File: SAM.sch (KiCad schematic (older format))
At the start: 60 parts, among them J301 CONN_02x05, 0.05\", SW301 Switch_DPST, SW302 Switch_DPST, U301 ATSAMD21J18A-MUT, U302 AAT4610, U303 AAT4610, X301 FC-135

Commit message: components and footprints
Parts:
- SW301, SW302: footprint (none) -> tm-kicad-lib:SPST-TH
- TP301, TP303, TP304, TP305, TP306, TP307, TP308, TP309, TP310, TP311, TP312, TP313, TP314, TP315, TP316, TP317, TP318, TP319, TP320, TP321, TP322, TP323, TP324: value 0914-0-15-20-77-14-11-0 -> 0932-0-15-20-77-14-11-0
- TP302: value 0914-0-15-20-77-14-11-0-0-15-20-77-14-11-0 -> 0932-0-15-20-77-14-11-0
- U302, U303: footprint (none) -> Housings_SOT-23_SOT-143_TSOT-6:SOT-23-5
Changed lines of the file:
@@
 P 8800 2300
 F 0 "TP322" H 8800 2350 60  0000 C CNN
-F 1 "0914-0-15-20-77-14-11-0" H 8800 2250 60  0001 C CNN
+F 1 "0932-0-15-20-77-14-11-0" H 8800 2250 60  0001 C CNN
 F 2 "tm-kicad-lib:Testpoint" H 8800 2300 60  0001 C CNN
 F 3 "" H 8800 2300 60  0000 C CNN
@@
 P 8800 2500
 F 0 "TP323" H 8800 2550 60  0000 C CNN
-F 1 "0914-0-15-20-77-14-11-0" H 8800 2450 60  0001 C CNN
+F 1 "0932-0-15-20-77-14-11-0" H 8800 2450 60  0001 C CNN
 F 2 "tm-kicad-lib:Testpoint" H 8800 2500 60  0001 C CNN
 F 3 "" H 8800 2500 60  0000 C CNN
@@
 P 8800 2100
 F 0 "TP321" H 8800 2150 60  0000 C CNN
-F 1 "0914-0-15-20-77-14-11-0" H 8800 2050 60  0001 C CNN
+F 1 "0932-0-15-20-77-14-11-0" H 8800 2050 60  0001 C CNN
 F 2 "tm-kicad-lib:Testpoint" H 8800 2100 60  0001 C CNN
 F 3 "" H 8800 2100 60  0000 C CNN
@@
 P 8800 1900
 F 0 "TP320" H 8800 1950 60  0000 C CNN
-F 1 "0914-0-15-20-77-14-11-0" H 8800 1850 60  0001 C CNN
+F 1 "0932-0-15-20-77-14-11-0" H 8800 1850 60  0001 C CNN
 F 2 "tm-kicad-lib:Testpoint" H 8800 1900 60  0001 C CNN
 F 3 "" H 8800 1900 60  0000 C CNN
@@
 P 8000 5500
 F 0 "TP302" H 8000 5550 60  0000 C CNN
-F 1 "0914-0-15-20-77-14-11-0-0-15-20-77-14-11-0" H 8000 5450 60  0001 C CNN
+F 1 "0932-0-15-20-77-14-11-0" H 8000 5450 60  0001 C CNN
 F 2 "tm-kicad-lib:Testpoint" H 8000 5500 60  0001 C CNN
 F 3 "" H 8000 5500 60  0000 C CNN
@@
 P 8000 5600
 F 0 "TP303" H 8000 5650 60  0000 C CNN
-F 1 "0914-0-15-20-77-14-11-0" H 8000 5550 60  0001 C CNN
+F 1 "0932-0-15-20-77-14-11-0" H 8000 5550 60  0001 C CNN
 F 2 "tm-kicad-lib:Testpoint" H 8000 5600 60  0001 C CNN
 F 3 "" H 8000 5600 60  0000 C CNN
@@
 P 8000 5800
 F 0 "TP305" H 8000 5850 60  0000 C CNN
-F 1 "0914-0-15-20-77-14-11-0" H 8000 5750 60  0001 C CNN
+F 1 "0932-0-15-20-77-14-11-0" H 8000 5750 60  0001 C CNN
 F 2 "tm-kicad-lib:Testpoint" H 8000 5800 60  0001 C CNN
 F 3 "" H 8000 5800 60  0000 C CNN
@@
 P 8000 6000
 F 0 "TP306" H 8000 6050 60  0000 C CNN
-F 1 "0914-0-15-20-77-14-11-0" H 8000 5950 60  0001 C CNN
+F 1 "0932-0-15-20-77-14-11-0" H 8000 5950 60  0001 C CNN
 F 2 "tm-kicad-lib:Testpoint" H 8000 6000 60  0001 C CNN
 F 3 "" H 8000 6000 60  0000 C CNN
@@
 P 8000 6100
 F 0 "TP307" H 8000 6150 60  0000 C CNN
-F 1 "0914-0-15-20-77-14-11-0" H 8000 6050 60  0001 C CNN
+F 1 "0932-0-15-20-77-14-11-0" H 8000 6050 60  0001 C CNN
 F 2 "tm-kicad-lib:Testpoint" H 8000 6100 60  0001 C CNN
 F 3 "" H 8000 6100 60  0000 C CNN
@@
 P 8000 6200
 F 0 "TP308" H 8000 6250 60  0000 C CNN
-F 1 "0914-0-15-20-77-14-11-0" H 8000 6150 60  0001 C CNN
+F 1 "0932-0-15-20-77-14-11-0" H 8000 6150 60  0001 C CNN
 F 2 "tm-kicad-lib:Testpoint" H 8000 6200 60  0001 C CNN
 F 3 "" H 8000 6200 60  0000 C CNN
@@
 P 8000 6300
 F 0 "TP309" H 8000 6350 60  0000 C CNN
-F 1 "0914-0-15-20-77-14-11-0" H 8000 6250 60  0001 C CNN
+F 1 "0932-0-15-20-77-14-11-0" H 8000 6250 60  0001 C CNN
 F 2 "tm-kicad-lib:Testpoint" H 8000 6300 60  0001 C CNN
 F 3 "" H 8000 6300 60  0000 C CNN
@@
 P 8000 6500
 F 0 "TP310" H 8000 6550 60  0000 C CNN
-F 1 "0914-0-15-20-77-14-11-0" H 8000 6450 60  0001 C CNN
+F 1 "0932-0-15-20-77-14-11-0" H 8000 6450 60  0001 C CNN
 F 2 "tm-kicad-lib:Testpoint" H 8000 6500 60  0001 C CNN
 F 3 "" H 8000 6500 60  0000 C CNN
@@
 P 8000 6600
 F 0 "TP311" H 8000 6650 60  0000 C CNN
-F 1 "0914-0-15-20-77-14-11-0" H 8000 6550 60  0001 C CNN
+F 1 "0932-0-15-20-77-14-11-0" H 8000 6550 60  0001 C CNN
 F 2 "tm-kicad-lib:Testpoint" H 8000 6600 60  0001 C CNN
 F 3 "" H 8000 6600 60  0000 C CNN
@@
 P 8000 6700
 F 0 "TP312" H 8000 6750 60  0000 C CNN
-F 1 "0914-0-15-20-77-14-11-0" H 8000 6650 60  0001 C CNN
+F 1 "0932-0-15-20-77-14-11-0" H 8000 6650 60  0001 C CNN
 F 2 "tm-kicad-lib:Testpoint" H 8000 6700 60  0001 C CNN
 F 3 "" H 8000 6700 60  0000 C CNN
@@
 P 8000 6800
 F 0 "TP313" H 8000 6850 60  0000 C CNN
-F 1 "0914-0-15-20-77-14-11-0" H 8000 6750 60  0001 C CNN
+F 1 "0932-0-15-20-77-14-11-0" H 8000 6750 60  0001 C CNN
 F 2 "tm-kicad-lib:Testpoint" H 8000 6800 60  0001 C CNN
 F 3 "" H 8000 6800 60  0000 C CNN
@@
 P 8000 8000
 F 0 "TP317" H 8000 8050 60  0000 C CNN
-F 1 "0914-0-15-20-77-14-11-0" H 8000 7950 60  0001 C CNN
+F 1 "0932-0-15-20-77-14-11-0" H 8000 7950 60  0001 C CNN
 F 2 "tm-kicad-lib:Testpoint" H 8000 8000 60  0001 C CNN
 F 3 "" H 8000 8000 60  0000 C CNN
@@
 P 8000 8100
 F 0 "TP318" H 8000 8150 60  0000 C CNN
-F 1 "0914-0-15-20-77-14-11-0" H 8000 8050 60  0001 C CNN
+F 1 "0932-0-15-20-77-14-11-0" H 8000 8050 60  0001 C CNN
 F 2 "tm-kicad-lib:Testpoint" H 8000 8100 60  0001 C CNN
 F 3 "" H 8000 8100 60  0000 C CNN
@@
 P 8000 7700
 F 0 "TP315" H 8000 7750 60  0000 C CNN
-F 1 "0914-0-15-20-77-14-11-0" H 8000 7650 60  0001 C CNN
+F 1 "0932-0-15-20-77-14-11-0" H 8000 7650 60  0001 C CNN
 F 2 "tm-kicad-lib:Testpoint" H 8000 7700 60  0001 C CNN
 F 3 "" H 8000 7700 60  0000 C CNN
@@
 P 8000 7800
 F 0 "TP316" H 8000 7850 60  0000 C CNN
-F 1 "0914-0-15-20-77-14-11-0" H 8000 7750 60  0001 C CNN
+F 1 "0932-0-15-20-77-14-11-0" H 8000 7750 60  0001 C CNN
 F 2 "tm-kicad-lib:Testpoint" H 8000 7800 60  0001 C CNN
 F 3 "" H 8000 7800 60  0000 C CNN
@@
 P 8000 7500
 F 0 "TP314" H 8000 7550 60  0000 C CNN
-F 1 "0914-0-15-20-77-14-11-0" H 8000 7450 60  0001 C CNN
+F 1 "0932-0-15-20-77-14-11-0" H 8000 7450 60  0001 C CNN
 F 2 "tm-kicad-lib:Testpoint" H 8000 7500 60  0001 C CNN
 F 3 "" H 8000 7500 60  0000 C CNN
@@
 P 2700 5900
 F 0 "TP301" H 2700 5950 60  0000 C CNN
-F 1 "0914-0-15-20-77-14-11-0" H 2700 5850 60  0001 C CNN
+F 1 "0932-0-15-20-77-14-11-0" H 2700 5850 60  0001 C CNN
 F 2 "tm-kicad-lib:Testpoint" H 2700 5900 60  0001 C CNN
 F 3 "" H 2700 5900 60  0000 C CNN
@@
 P 8000 5700
 F 0 "TP304" H 8000 5750 60  0000 C CNN
-F 1 "0914-0-15-20-77-14-11-0" H 8000 5650 60  0001 C CNN
+F 1 "0932-0-15-20-77-14-11-0" H 8000 5650 60  0001 C CNN
 F 2 "tm-kicad-lib:Testpoint" H 8000 5700 60  0001 C CNN
 F 3 "" H 8000 5700 60  0000 C CNN
@@
 F 0 "U302" H 14450 5750 60  0000 C CNN
 F 1 "AAT4610" H 14800 5500 60  0000 C CNN
-F 2 "" H 14800 5500 60  0000 C CNN
+F 2 "Housings_SOT-23_SOT-143_TSOT-6:SOT-23-5" H 14800 5500 60  0001 C CNN
 F 3 "" H 14800 5500 60  0000 C CNN
 	1    14800 5500
@@
 F 0 "U303" H 14450 7450 60  0000 C CNN
 F 1 "AAT4610" H 14800 7200 60  0000 C CNN
-F 2 "" H 14800 7200 60  0000 C CNN
+F 2 "Housings_SOT-23_SOT-143_TSOT-6:SOT-23-5" H 14800 7200 60  0001 C CNN
 F 3 "" H 14800 7200 60  0000 C CNN
 	1    14800 7200
@@
 P 16100 6800
 F 0 "TP324" H 16100 6850 60  0000 C CNN
-F 1 "0914-0-15-20-77-14-11-0" H 16100 6750 60  0001 C CNN
-F 2 "" H 16100 6800 60  0000 C CNN
+F 1 "0932-0-15-20-77-14-11-0" H 16100 6750 60  0001 C CNN
+F 2 "" H 16100 6800 60  0001 C CNN
 F 3 "" H 16100 6800 60  0000 C CNN
 	1    16100 6800
@@
 P 8000 8400
 F 0 "TP319" H 8000 8450 60  0000 C CNN
-F 1 "0914-0-15-20-77-14-11-0" H 8000 8350 60  0001 C CNN
+F 1 "0932-0-15-20-77-14-11-0" H 8000 8350 60  0001 C CNN
 F 2 "tm-kicad-lib:Testpoint" H 8000 8400 60  0001 C CNN
 F 3 "" H 8000 8400 60  0000 C CNN
@@
 F 0 "SW301" H 10700 2650 50  0000 C CNN
 F 1 "Switch_DPST" H 10700 2550 50  0000 C CNN
-F 2 "" H 10400 2600 60  0000 C CNN
+F 2 "tm-kicad-lib:SPST-TH" H 10400 2600 60  0001 C CNN
 F 3 "" H 10400 2600 60  0000 C CNN
 	1    10400 2600
@@
 F 0 "SW302" H 14000 2650 50  0000 C CNN
 F 1 "Switch_DPST" H 14000 2550 50  0000 C CNN
-F 2 "" H 13700 2600 60  0000 C CNN
+F 2 "tm-kicad-lib:SPST-TH" H 13700 2600 60  0001 C CNN
 F 3 "" H 13700 2600 60  0000 C CNN
 	1    13700 2600

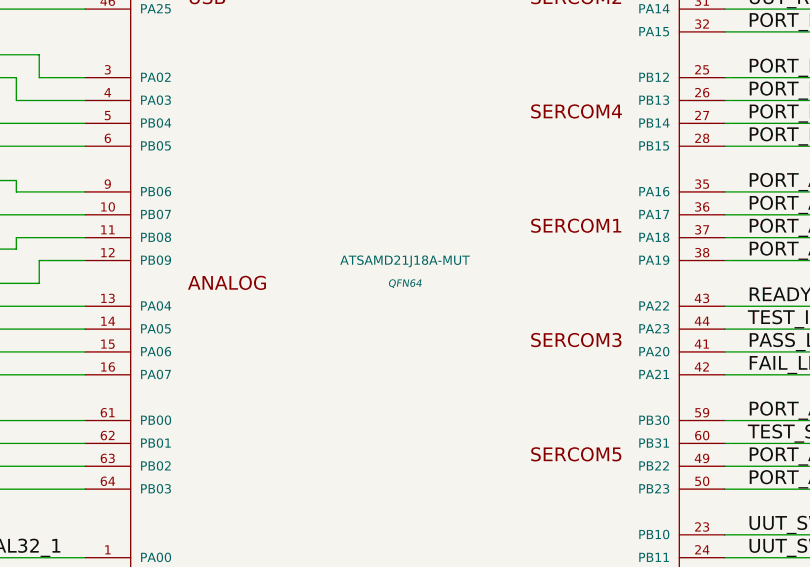
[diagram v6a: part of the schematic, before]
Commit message: swapped testpoints
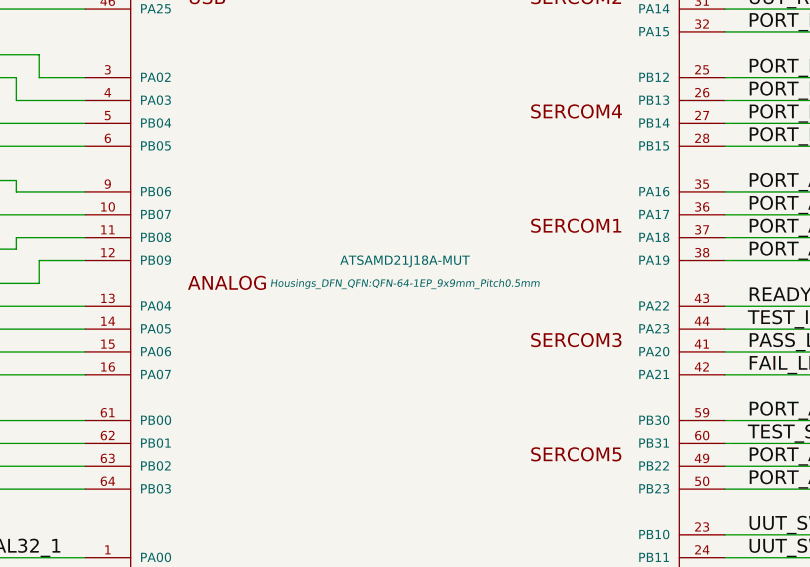
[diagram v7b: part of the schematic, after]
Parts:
- TP301, TP302, TP303, TP304, TP305, TP306, TP307, TP308, TP309, TP310, TP311, TP312, TP313, TP314, TP315, TP316, TP317, TP318, TP319, TP320, TP321, TP322, TP323: footprint tm-kicad-lib:Testpoint -> tm-kicad-lib:0932-0-15-20-77-14-11-0
- TP324: footprint (none) -> tm-kicad-lib:0932-0-15-20-77-14-11-0
- U301: footprint QFN64 -> Housings_DFN_QFN:QFN-64-1EP_9x9mm_Pitch0.5mm
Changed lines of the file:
@@
 F 0 "TP322" H 8800 2350 60  0000 C CNN
 F 1 "0932-0-15-20-77-14-11-0" H 8800 2250 60  0001 C CNN
-F 2 "tm-kicad-lib:Testpoint" H 8800 2300 60  0001 C CNN
+F 2 "tm-kicad-lib:0932-0-15-20-77-14-11-0" H 8800 2300 60  0001 C CNN
 F 3 "" H 8800 2300 60  0000 C CNN
 	1    8800 2300
@@
 F 0 "TP323" H 8800 2550 60  0000 C CNN
 F 1 "0932-0-15-20-77-14-11-0" H 8800 2450 60  0001 C CNN
-F 2 "tm-kicad-lib:Testpoint" H 8800 2500 60  0001 C CNN
+F 2 "tm-kicad-lib:0932-0-15-20-77-14-11-0" H 8800 2500 60  0001 C CNN
 F 3 "" H 8800 2500 60  0000 C CNN
 	1    8800 2500
@@
 F 0 "TP321" H 8800 2150 60  0000 C CNN
 F 1 "0932-0-15-20-77-14-11-0" H 8800 2050 60  0001 C CNN
-F 2 "tm-kicad-lib:Testpoint" H 8800 2100 60  0001 C CNN
+F 2 "tm-kicad-lib:0932-0-15-20-77-14-11-0" H 8800 2100 60  0001 C CNN
 F 3 "" H 8800 2100 60  0000 C CNN
 	1    8800 2100
@@
 F 0 "TP320" H 8800 1950 60  0000 C CNN
 F 1 "0932-0-15-20-77-14-11-0" H 8800 1850 60  0001 C CNN
-F 2 "tm-kicad-lib:Testpoint" H 8800 1900 60  0001 C CNN
+F 2 "tm-kicad-lib:0932-0-15-20-77-14-11-0" H 8800 1900 60  0001 C CNN
 F 3 "" H 8800 1900 60  0000 C CNN
 	1    8800 1900
@@
 F 0 "U301" H 4200 8850 40  0000 C CNN
 F 1 "ATSAMD21J18A-MUT" H 5300 6800 40  0000 C CNN
-F 2 "QFN64" H 5300 6700 32  0000 C CIN
+F 2 "Housings_DFN_QFN:QFN-64-1EP_9x9mm_Pitch0.5mm" H 5300 6700 32  0000 C CIN
 F 3 "" H 4100 6450 60  0000 C CNN
 	1    5300 6800
@@
 F 0 "TP302" H 8000 5550 60  0000 C CNN
 F 1 "0932-0-15-20-77-14-11-0" H 8000 5450 60  0001 C CNN
-F 2 "tm-kicad-lib:Testpoint" H 8000 5500 60  0001 C CNN
+F 2 "tm-kicad-lib:0932-0-15-20-77-14-11-0" H 8000 5500 60  0001 C CNN
 F 3 "" H 8000 5500 60  0000 C CNN
 	1    8000 5500
@@
 F 0 "TP303" H 8000 5650 60  0000 C CNN
 F 1 "0932-0-15-20-77-14-11-0" H 8000 5550 60  0001 C CNN
-F 2 "tm-kicad-lib:Testpoint" H 8000 5600 60  0001 C CNN
+F 2 "tm-kicad-lib:0932-0-15-20-77-14-11-0" H 8000 5600 60  0001 C CNN
 F 3 "" H 8000 5600 60  0000 C CNN
 	1    8000 5600
@@
 F 0 "TP305" H 8000 5850 60  0000 C CNN
 F 1 "0932-0-15-20-77-14-11-0" H 8000 5750 60  0001 C CNN
-F 2 "tm-kicad-lib:Testpoint" H 8000 5800 60  0001 C CNN
+F 2 "tm-kicad-lib:0932-0-15-20-77-14-11-0" H 8000 5800 60  0001 C CNN
 F 3 "" H 8000 5800 60  0000 C CNN
 	1    8000 5800
@@
 F 0 "TP306" H 8000 6050 60  0000 C CNN
 F 1 "0932-0-15-20-77-14-11-0" H 8000 5950 60  0001 C CNN
-F 2 "tm-kicad-lib:Testpoint" H 8000 6000 60  0001 C CNN
+F 2 "tm-kicad-lib:0932-0-15-20-77-14-11-0" H 8000 6000 60  0001 C CNN
 F 3 "" H 8000 6000 60  0000 C CNN
 	1    8000 6000
@@
 F 0 "TP307" H 8000 6150 60  0000 C CNN
 F 1 "0932-0-15-20-77-14-11-0" H 8000 6050 60  0001 C CNN
-F 2 "tm-kicad-lib:Testpoint" H 8000 6100 60  0001 C CNN
+F 2 "tm-kicad-lib:0932-0-15-20-77-14-11-0" H 8000 6100 60  0001 C CNN
 F 3 "" H 8000 6100 60  0000 C CNN
 	1    8000 6100
@@
 F 0 "TP308" H 8000 6250 60  0000 C CNN
 F 1 "0932-0-15-20-77-14-11-0" H 8000 6150 60  0001 C CNN
-F 2 "tm-kicad-lib:Testpoint" H 8000 6200 60  0001 C CNN
+F 2 "tm-kicad-lib:0932-0-15-20-77-14-11-0" H 8000 6200 60  0001 C CNN
 F 3 "" H 8000 6200 60  0000 C CNN
 	1    8000 6200
@@
 F 0 "TP309" H 8000 6350 60  0000 C CNN
 F 1 "0932-0-15-20-77-14-11-0" H 8000 6250 60  0001 C CNN
-F 2 "tm-kicad-lib:Testpoint" H 8000 6300 60  0001 C CNN
+F 2 "tm-kicad-lib:0932-0-15-20-77-14-11-0" H 8000 6300 60  0001 C CNN
 F 3 "" H 8000 6300 60  0000 C CNN
 	1    8000 6300
@@
 F 0 "TP310" H 8000 6550 60  0000 C CNN
 F 1 "0932-0-15-20-77-14-11-0" H 8000 6450 60  0001 C CNN
-F 2 "tm-kicad-lib:Testpoint" H 8000 6500 60  0001 C CNN
+F 2 "tm-kicad-lib:0932-0-15-20-77-14-11-0" H 8000 6500 60  0001 C CNN
 F 3 "" H 8000 6500 60  0000 C CNN
 	1    8000 6500
@@
 F 0 "TP311" H 8000 6650 60  0000 C CNN
 F 1 "0932-0-15-20-77-14-11-0" H 8000 6550 60  0001 C CNN
-F 2 "tm-kicad-lib:Testpoint" H 8000 6600 60  0001 C CNN
+F 2 "tm-kicad-lib:0932-0-15-20-77-14-11-0" H 8000 6600 60  0001 C CNN
 F 3 "" H 8000 6600 60  0000 C CNN
 	1    8000 6600
@@
 F 0 "TP312" H 8000 6750 60  0000 C CNN
 F 1 "0932-0-15-20-77-14-11-0" H 8000 6650 60  0001 C CNN
-F 2 "tm-kicad-lib:Testpoint" H 8000 6700 60  0001 C CNN
+F 2 "tm-kicad-lib:0932-0-15-20-77-14-11-0" H 8000 6700 60  0001 C CNN
 F 3 "" H 8000 6700 60  0000 C CNN
 	1    8000 6700
@@
 F 0 "TP313" H 8000 6850 60  0000 C CNN
 F 1 "0932-0-15-20-77-14-11-0" H 8000 6750 60  0001 C CNN
-F 2 "tm-kicad-lib:Testpoint" H 8000 6800 60  0001 C CNN
+F 2 "tm-kicad-lib:0932-0-15-20-77-14-11-0" H 8000 6800 60  0001 C CNN
 F 3 "" H 8000 6800 60  0000 C CNN
 	1    8000 6800
@@
 F 0 "TP317" H 8000 8050 60  0000 C CNN
 F 1 "0932-0-15-20-77-14-11-0" H 8000 7950 60  0001 C CNN
-F 2 "tm-kicad-lib:Testpoint" H 8000 8000 60  0001 C CNN
+F 2 "tm-kicad-lib:0932-0-15-20-77-14-11-0" H 8000 8000 60  0001 C CNN
 F 3 "" H 8000 8000 60  0000 C CNN
 	1    8000 8000
@@
 F 0 "TP318" H 8000 8150 60  0000 C CNN
 F 1 "0932-0-15-20-77-14-11-0" H 8000 8050 60  0001 C CNN
-F 2 "tm-kicad-lib:Testpoint" H 8000 8100 60  0001 C CNN
+F 2 "tm-kicad-lib:0932-0-15-20-77-14-11-0" H 8000 8100 60  0001 C CNN
 F 3 "" H 8000 8100 60  0000 C CNN
 	1    8000 8100
@@
 F 0 "TP315" H 8000 7750 60  0000 C CNN
 F 1 "0932-0-15-20-77-14-11-0" H 8000 7650 60  0001 C CNN
-F 2 "tm-kicad-lib:Testpoint" H 8000 7700 60  0001 C CNN
+F 2 "tm-kicad-lib:0932-0-15-20-77-14-11-0" H 8000 7700 60  0001 C CNN
 F 3 "" H 8000 7700 60  0000 C CNN
 	1    8000 7700
@@
 F 0 "TP316" H 8000 7850 60  0000 C CNN
 F 1 "0932-0-15-20-77-14-11-0" H 8000 7750 60  0001 C CNN
-F 2 "tm-kicad-lib:Testpoint" H 8000 7800 60  0001 C CNN
+F 2 "tm-kicad-lib:0932-0-15-20-77-14-11-0" H 8000 7800 60  0001 C CNN
 F 3 "" H 8000 7800 60  0000 C CNN
 	1    8000 7800
@@
 F 0 "TP314" H 8000 7550 60  0000 C CNN
 F 1 "0932-0-15-20-77-14-11-0" H 8000 7450 60  0001 C CNN
-F 2 "tm-kicad-lib:Testpoint" H 8000 7500 60  0001 C CNN
+F 2 "tm-kicad-lib:0932-0-15-20-77-14-11-0" H 8000 7500 60  0001 C CNN
 F 3 "" H 8000 7500 60  0000 C CNN
 	1    8000 7500
@@
 F 0 "TP301" H 2700 5950 60  0000 C CNN
 F 1 "0932-0-15-20-77-14-11-0" H 2700 5850 60  0001 C CNN
-F 2 "tm-kicad-lib:Testpoint" H 2700 5900 60  0001 C CNN
+F 2 "tm-kicad-lib:0932-0-15-20-77-14-11-0" H 2700 5900 60  0001 C CNN
 F 3 "" H 2700 5900 60  0000 C CNN
 	1    2700 5900
@@
 F 0 "TP304" H 8000 5750 60  0000 C CNN
 F 1 "0932-0-15-20-77-14-11-0" H 8000 5650 60  0001 C CNN
-F 2 "tm-kicad-lib:Testpoint" H 8000 5700 60  0001 C CNN
+F 2 "tm-kicad-lib:0932-0-15-20-77-14-11-0" H 8000 5700 60  0001 C CNN
 F 3 "" H 8000 5700 60  0000 C CNN
 	1    8000 5700
@@
 F 0 "TP324" H 16100 6850 60  0000 C CNN
 F 1 "0932-0-15-20-77-14-11-0" H 16100 6750 60  0001 C CNN
-F 2 "" H 16100 6800 60  0001 C CNN
+F 2 "tm-kicad-lib:0932-0-15-20-77-14-11-0" H 16100 6800 60  0001 C CNN
 F 3 "" H 16100 6800 60  0000 C CNN
 	1    16100 6800
@@
 F 0 "TP319" H 8000 8450 60  0000 C CNN
 F 1 "0932-0-15-20-77-14-11-0" H 8000 8350 60  0001 C CNN
-F 2 "tm-kicad-lib:Testpoint" H 8000 8400 60  0001 C CNN
+F 2 "tm-kicad-lib:0932-0-15-20-77-14-11-0" H 8000 8400 60  0001 C CNN
 F 3 "" H 8000 8400 60  0000 C CNN
 	1    8000 8400

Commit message: on to layout! and what an adventure it will be...
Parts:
- removed TP320, TP322, TP323: 0932-0-15-20-77-14-11-0, tm-kicad-lib:0932-0-15-20-77-14-11-0, symbol TP
- added TP325, TP326, TP327, TP328: 0932-0-15-20-77-14-11-0, tm-kicad-lib:0932-0-15-20-77-14-11-0, symbol TP
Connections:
- wire segments 206 -> 204
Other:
- moved on the sheet: TP321
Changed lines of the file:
@@
 	1    0    0    -1
 $EndComp
-Text GLabel 8800 2800 2    60   BiDi ~ 0
+Text GLabel 8500 2800 2    60   BiDi ~ 0
 SWDIO
-Text GLabel 8800 3000 2    60   Input ~ 0
+Text GLabel 8500 3000 2    60   Input ~ 0
 SWCLK
 Text GLabel 8500 3300 2    60   Input ~ 0
@@
 12.5pF\nNOMINAL\nSHUNT
 $Comp
-L TP TP322
-U 1 1 55076899
-P 8800 2300
-F 0 "TP322" H 8800 2350 60  0000 C CNN
-F 1 "0932-0-15-20-77-14-11-0" H 8800 2250 60  0001 C CNN
-F 2 "tm-kicad-lib:0932-0-15-20-77-14-11-0" H 8800 2300 60  0001 C CNN
-F 3 "" H 8800 2300 60  0000 C CNN
-	1    8800 2300
-	1    0    0    1
-$EndComp
-$Comp
-L TP TP323
-U 1 1 55076939
-P 8800 2500
-F 0 "TP323" H 8800 2550 60  0000 C CNN
-F 1 "0932-0-15-20-77-14-11-0" H 8800 2450 60  0001 C CNN
-F 2 "tm-kicad-lib:0932-0-15-20-77-14-11-0" H 8800 2500 60  0001 C CNN
-F 3 "" H 8800 2500 60  0000 C CNN
-	1    8800 2500
-	1    0    0    1
-$EndComp
-$Comp
 L TP TP321
 U 1 1 550772D3
-P 8800 2100
-F 0 "TP321" H 8800 2150 60  0000 C CNN
-F 1 "0932-0-15-20-77-14-11-0" H 8800 2050 60  0001 C CNN
-F 2 "tm-kicad-lib:0932-0-15-20-77-14-11-0" H 8800 2100 60  0001 C CNN
-F 3 "" H 8800 2100 60  0000 C CNN
-	1    8800 2100
-	1    0    0    1
+P 8350 7900
+F 0 "TP321" H 8350 7950 60  0000 C CNN
+F 1 "0932-0-15-20-77-14-11-0" H 8350 7850 60  0001 C CNN
+F 2 "tm-kicad-lib:0932-0-15-20-77-14-11-0" H 8350 7900 60  0001 C CNN
+F 3 "" H 8350 7900 60  0000 C CNN
+	1    8350 7900
+	0    1    -1   0
 $EndComp
 $Comp
 L GND #PWR067
 U 1 1 55077307
-P 8200 2200
-F 0 "#PWR067" H 8200 1950 60  0001 C CNN
-F 1 "GND" H 8200 2050 60  0000 C CNN
-F 2 "" H 8200 2200 60  0000 C CNN
-F 3 "" H 8200 2200 60  0000 C CNN
-	1    8200 2200
-	1    0    0    -1
-$EndComp
-$Comp
-L TP TP320
-U 1 1 5507734C
-P 8800 1900
-F 0 "TP320" H 8800 1950 60  0000 C CNN
-F 1 "0932-0-15-20-77-14-11-0" H 8800 1850 60  0001 C CNN
-F 2 "tm-kicad-lib:0932-0-15-20-77-14-11-0" H 8800 1900 60  0001 C CNN
-F 3 "" H 8800 1900 60  0000 C CNN
-	1    8800 1900
-	1    0    0    1
+P 8350 8100
+F 0 "#PWR067" H 8350 7850 60  0001 C CNN
+F 1 "GND" H 8350 7950 60  0000 C CNN
+F 2 "" H 8350 8100 60  0000 C CNN
+F 3 "" H 8350 8100 60  0000 C CNN
+	1    8350 8100
+	1    0    0    -1
 $EndComp
 $Comp
@@
 F 3 "" H 7600 2800 60  0000 C CNN
 	1    7600 2800
-	1    0    0    -1
-$EndComp
-$Comp
-L +3.3V #PWR069
-U 1 1 5536E990
-P 8400 1800
-F 0 "#PWR069" H 8400 1650 50  0001 C CNN
-F 1 "+3.3V" H 8400 1940 50  0000 C CNN
-F 2 "" H 8400 1800 60  0000 C CNN
-F 3 "" H 8400 1800 60  0000 C CNN
-	1    8400 1800
 	1    0    0    -1
 $EndComp
@@
 	3600 5600 3600 5550
 Wire Wire Line
-	8400 1800 8400 1900
-Wire Wire Line
 	8000 7600 6700 7600
-Wire Wire Line
-	8200 2100 8200 2200
-Wire Wire Line
-	8800 2100 8200 2100
-Wire Wire Line
-	8400 1900 8800 1900
-Wire Wire Line
-	8800 2500 8500 2500
-Wire Wire Line
-	8800 2300 8400 2300
 Wire Wire Line
 	2900 4000 2900 3900
@@
 	8500 3300 8300 3300
 Wire Wire Line
-	8300 3000 8800 3000
-Wire Wire Line
-	8300 2900 8700 2900
+	8300 3000 8500 3000
+Wire Wire Line
+	8300 2900 8400 2900
 Wire Wire Line
 	7600 2900 7600 2800
@@
 	7800 2900 7600 2900
 Wire Wire Line
-	8500 2500 8500 3000
-Connection ~ 8500 3000
-Wire Wire Line
-	8400 2300 8400 2900
-Connection ~ 8400 2900
-Wire Wire Line
-	8700 2900 8700 2800
-Wire Wire Line
-	8700 2800 8800 2800
+	8400 2900 8400 2800
+Wire Wire Line
+	8400 2800 8500 2800
 Wire Wire Line
 	8000 8100 6700 8100
@@
 Wire Wire Line
 	6700 8400 8000 8400
+$Comp
+L TP TP325
+U 1 1 55487FF4
+P 8900 3800
+F 0 "TP325" H 8900 3850 60  0000 C CNN
+F 1 "0932-0-15-20-77-14-11-0" H 8900 3750 60  0001 C CNN
+F 2 "tm-kicad-lib:0932-0-15-20-77-14-11-0" H 8900 3800 60  0001 C CNN
+F 3 "" H 8900 3800 60  0000 C CNN
+	1    8900 3800
+	1    0    0    1
+$EndComp
+$Comp
+L TP TP326
+U 1 1 55488045
+P 8900 4000
+F 0 "TP326" H 8900 4050 60  0000 C CNN
+F 1 "0932-0-15-20-77-14-11-0" H 8900 3950 60  0001 C CNN
+F 2 "tm-kicad-lib:0932-0-15-20-77-14-11-0" H 8900 4000 60  0001 C CNN
+F 3 "" H 8900 4000 60  0000 C CNN
+	1    8900 4000
+	1    0    0    1
+$EndComp
+$Comp
+L TP TP327
+U 1 1 554880AD
+P 8900 4200
+F 0 "TP327" H 8900 4250 60  0000 C CNN
+F 1 "0932-0-15-20-77-14-11-0" H 8900 4150 60  0001 C CNN
+F 2 "tm-kicad-lib:0932-0-15-20-77-14-11-0" H 8900 4200 60  0001 C CNN
+F 3 "" H 8900 4200 60  0000 C CNN
+	1    8900 4200
+	1    0    0    1
+$EndComp
+$Comp
+L TP TP328
+U 1 1 554880B3
+P 8900 4400
+F 0 "TP328" H 8900 4450 60  0000 C CNN
+F 1 "0932-0-15-20-77-14-11-0" H 8900 4350 60  0001 C CNN
+F 2 "tm-kicad-lib:0932-0-15-20-77-14-11-0" H 8900 4400 60  0001 C CNN
+F 3 "" H 8900 4400 60  0000 C CNN
+	1    8900 4400
+	1    0    0    1
+$EndComp
+Wire Wire Line
+	8900 3800 8700 3800
+Wire Wire Line
+	8700 3800 8700 4600
+Wire Wire Line
+	8900 4400 8700 4400
+Connection ~ 8700 4400
+Wire Wire Line
+	8900 4200 8700 4200
+Connection ~ 8700 4200
+Wire Wire Line
+	8900 4000 8700 4000
+Connection ~ 8700 4000
+$Comp
+L GND #PWR090
+U 1 1 554885D5
+P 8700 4600
+F 0 "#PWR090" H 8700 4350 60  0001 C CNN
+F 1 "GND" H 8700 4450 60  0000 C CNN
+F 2 "" H 8700 4600 60  0000 C CNN
+F 3 "" H 8700 4600 60  0000 C CNN
+	1    8700 4600
+	1    0    0    -1
+$EndComp
+Wire Wire Line
+	8350 7900 8350 8100
 $EndSCHEMATC
